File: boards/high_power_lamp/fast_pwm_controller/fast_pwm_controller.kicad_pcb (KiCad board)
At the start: 2 copper layers, 74 parts, among them J1 Screw_Terminal_01x02, J2 Screw_Terminal_01x02, J3 Screw_Terminal_01x02, J4 Screw_Terminal_01x02, J5 Screw_Terminal_01x02, J6 Screw_Terminal_01x02, J7 Screw_Terminal_01x02, J8 Screw_Terminal_01x02, J9 Screw_Terminal_01x02, Q1 BUK7516-55A,127, Q2 BUK7516-55A,127, Q3 BUK7516-55A,127, Q4 BUK7516-55A,127, U1 4050, U2 TLC3704, U3 SPX5205-adjustable, U4 ADA4851-4, U5 LMR380(10/20)

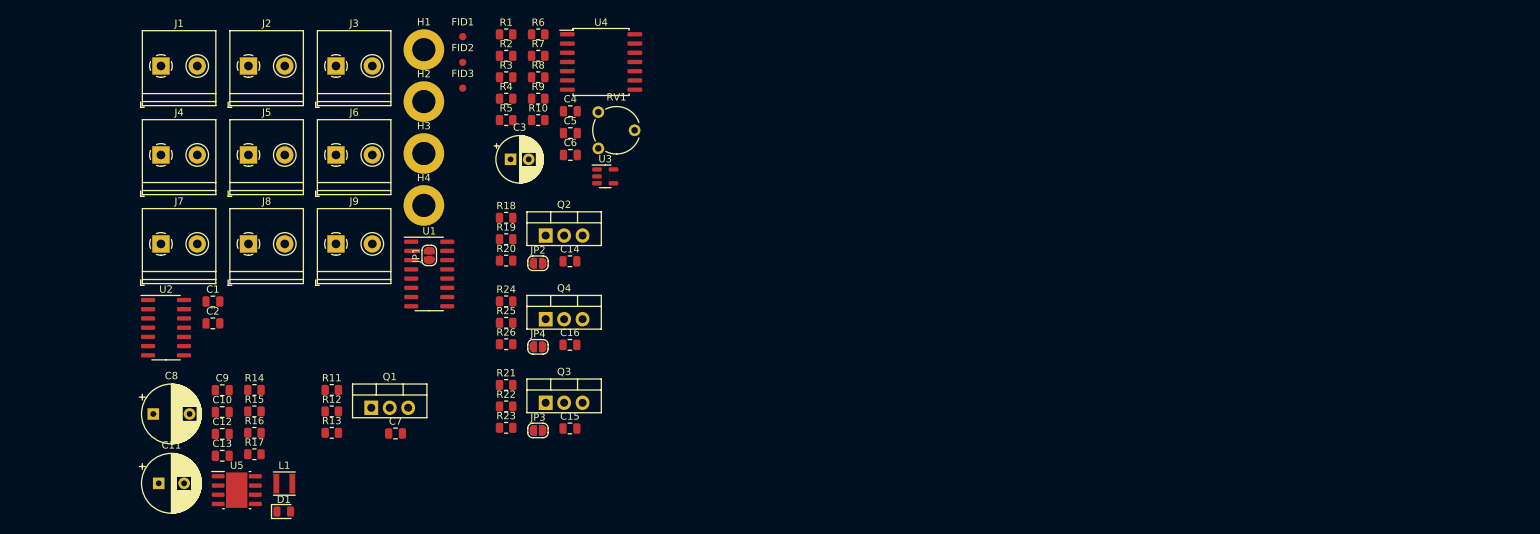
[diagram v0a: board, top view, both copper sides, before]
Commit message: buck converter can now be switched off via jumper
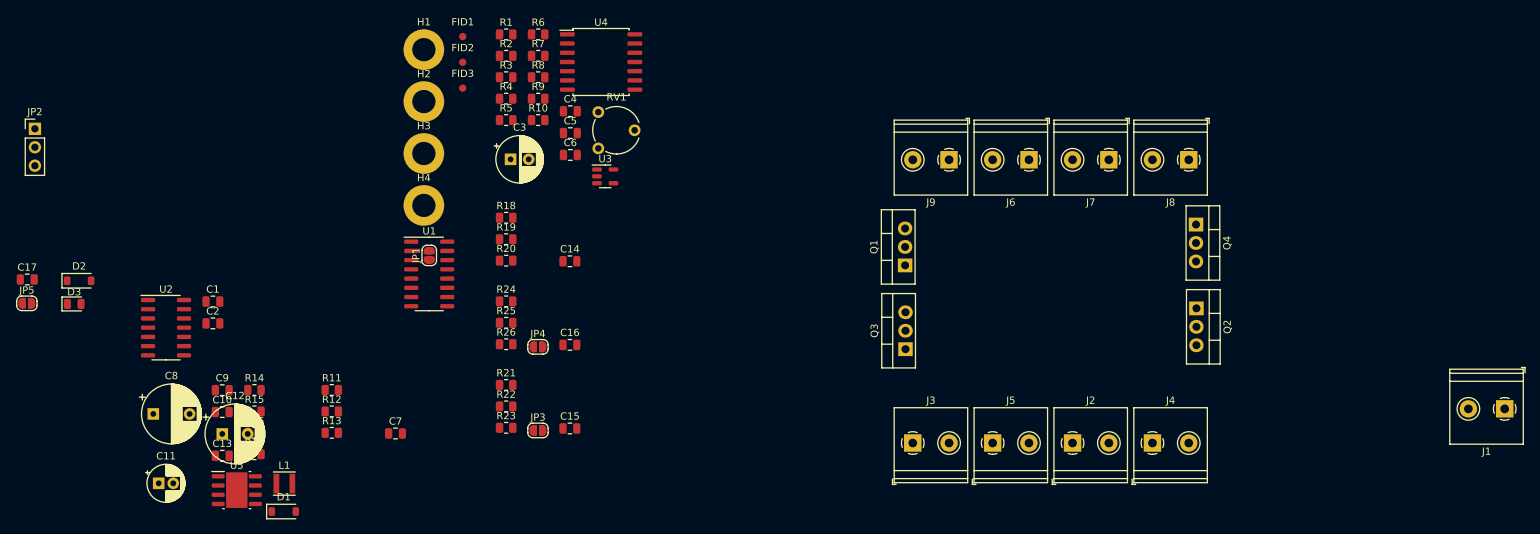
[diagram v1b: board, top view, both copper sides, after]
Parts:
- added C17: 500nF, Capacitor_SMD:C_0805_2012Metric, F.Cu at (43.1, 86.5)
- added D2: 1N4148, Diode_SMD:D_SOD-123, F.Cu at (50.2, 86.7)
- added D3: GREEN LED, LED_SMD:LED_0805_2012Metric, F.Cu at (49.5, 89.9)
- added JP5: SolderJumper_2_Open, Jumper:SolderJumper-2_P1.3mm_Open_RoundedPad1.0x1.5mm, F.Cu at (43.0, 89.8)
- C11: value 220μ -> 22μ; footprint Capacitor_THT:CP_Radial_D8.0mm_P3.50mm -> Capacitor_THT:CP_Radial_D5.0mm_P2.00mm
- C12: value 1μ -> 220μ; footprint Capacitor_SMD:C_0805_2012Metric -> Capacitor_THT:CP_Radial_D8.0mm_P3.50mm
- C13: value 100n -> 1μ
- C14: value 500nF -> 100n
- D1: value GREEN LED -> 1N4148; footprint LED_SMD:LED_0805_2012Metric -> Diode_SMD:D_SOD-123
- JP2: value SolderJumper_2_Open -> Jumper_3; footprint Jumper:SolderJumper-2_P1.3mm_Open_RoundedPad1.0x1.5mm -> Connector_PinHeader_2.54mm:PinHeader_1x03_P2.54mm_Vertical
- R15: value 100k -> 120k
- R16: value 9.09k -> 10.2k
- moved J1 190.9 mm to (246.5, 104.3), turned to 180 degrees
- moved J4 142.2 mm to (198.0, 109.0)
- moved J7 131.0 mm to (192.0, 70.0), turned to 180 degrees
- moved J8 130.0 mm to (203.0, 70.0), turned to 180 degrees
- moved J2 124.8 mm to (187.0, 109.0)
- moved J5 109.9 mm to (176.0, 109.0)
- moved J6 95.4 mm to (181.0, 70.0), turned to 180 degrees
- moved J3 94.9 mm to (165.0, 109.0)
- moved Q4 90.5 mm to (204.0, 78.9), turned to -90 degrees
- moved Q2 90.2 mm to (204.1, 90.5), turned to -90 degrees
- moved J9 85.2 mm to (170.0, 70.0), turned to 180 degrees
- moved Q1 76.1 mm to (163.9, 84.5), turned to 90 degrees
- moved JP2 71.7 mm to (44.1, 65.7)
- moved Q3 50.1 mm to (164.0, 96.1), turned to 90 degrees
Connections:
- C11 pad 1: +12V -> Net-(D2-A)
- C14 pad 1: GND -> +12V
- C14 pad 2: Net-(U2B-+) -> GND
- C15 pad 2: Net-(U2C-+) -> Net-(U2B-+)
- C16 pad 2: Net-(U2D-+) -> Net-(U2C-+)
- C8 pad 1: VPP -> Net-(D1-K)
- C9 pad 1: VPP -> Net-(JP2-A)
- D1 pad 1: GND -> Net-(D1-K)
- D1 pad 2: Net-(D1-A) -> VPP
- JP2 pad 1: /PWM stage 2/IN -> Net-(JP2-A)
- JP2 pad 2: Net-(JP2-B) -> Net-(D1-K)
- JP3 pad 1: /PWM stage 3/IN -> /PWM stage 2/IN
- JP4 pad 1: /PWM stage 4/IN -> /PWM stage 3/IN
- L1 pad 2: +12V -> Net-(D2-A)
- R15 pad 2: +12V -> Net-(D2-A)
- R17 pad 1: Net-(D1-A) -> Net-(D3-A)
- R19 pad 2: Net-(JP2-B) -> Net-(JP3-B)
- R22 pad 2: Net-(JP3-B) -> Net-(JP4-B)
- R25 pad 2: Net-(JP4-B) -> Net-(JP5-B)
- U1 pad 10: Net-(JP4-B) -> Net-(JP5-B)
- U1 pad 4: Net-(JP2-B) -> Net-(JP3-B)
- U1 pad 6: Net-(JP3-B) -> Net-(JP4-B)
- U5 pad 2: VPP -> Net-(JP2-A)
- U5 pad 3: VPP -> Net-(JP2-A)

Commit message: basic external layout of board
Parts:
- added H5: MountingHole, MountingHole:MountingHole_3.2mm_M3_DIN965_Pad, F.Cu at (50.0, 50.0)
- added H6: MountingHole, MountingHole:MountingHole_3.2mm_M3_DIN965_Pad, F.Cu at (50.0, 112.0)
- added H7: MountingHole, MountingHole:MountingHole_3.2mm_M3_DIN965_Pad, F.Cu at (112.0, 50.0)
- added H8: MountingHole, MountingHole:MountingHole_3.2mm_M3_DIN965_Pad, F.Cu at (112.0, 112.0)
- moved C3 199.9 mm to (199.7, -108.5)
- moved C7 199.9 mm to (183.9, -70.7)
- moved C8 199.9 mm to (150.5, -73.4)
- moved D2 199.9 mm to (140.3, -91.8)
- moved FID3 199.9 mm to (193.2, -118.3)
- moved JP2 199.9 mm to (134.2, -112.7)
- moved JP5 199.9 mm to (133.1, -88.7)
- moved L1 199.9 mm to (168.6, -63.8)
- moved R11 199.9 mm to (175.1, -76.7)
- moved U2 199.9 mm to (152.3, -85.3)
- moved C11 199.9 mm to (151.3, -63.9)
- moved C13 199.9 mm to (160.0, -67.7)
- moved C4 199.9 mm to (208.0, -115.1)
- moved FID1 199.9 mm to (193.2, -125.4)
- moved FID2 199.9 mm to (193.2, -121.8)
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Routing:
- net VPP: track 0.00 -> 61.3 mm
- net /PWM stage 1/OUT: track 0.00 -> 49.1 mm
- net /PWM stage 2/OUT: track 0.00 -> 40.2 mm
- net /PWM stage 4/OUT: track 0.00 -> 23.5 mm
- net /PWM stage 3/OUT: track 0.00 -> 17.4 mm
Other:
- board outline added: 72 x 72 mm

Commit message: almost finish arranging the fast pwm controller pcb
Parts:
- added C18: 500nF, Capacitor_SMD:C_0805_2012Metric, F.Cu at (80.6, 84.1)
- C11: value 22μ -> 100n; footprint Capacitor_THT:CP_Radial_D5.0mm_P2.00mm -> Capacitor_SMD:C_0805_2012Metric
- C12: value 220μ -> 22μ; footprint Capacitor_THT:CP_Radial_D8.0mm_P3.50mm -> Capacitor_THT:CP_Radial_D5.0mm_P2.00mm
- C13: value 1μ -> 220μ; footprint Capacitor_SMD:C_0805_2012Metric -> Capacitor_THT:CP_Radial_D8.0mm_P3.50mm
- C14: value 100n -> 1μ
- C15: value 500nF -> 100n
- C3: value 100μF -> 100nF; footprint Capacitor_THT:CP_Radial_D6.3mm_P2.50mm -> Capacitor_SMD:C_0805_2012Metric
- C4: value 100nF -> 100μF; footprint Capacitor_SMD:C_0805_2012Metric -> Capacitor_THT:CP_Radial_D6.3mm_P2.50mm
- C6: value 1nF -> 100nF
- C7: value 500nF -> 1nF
- C8: value 100μ -> 500nF; footprint Capacitor_THT:CP_Radial_D8.0mm_P5.00mm -> Capacitor_SMD:C_0805_2012Metric
- C9: value 100n -> 100μ; footprint Capacitor_SMD:C_0805_2012Metric -> Capacitor_THT:CP_Radial_D8.0mm_P5.00mm
- moved FID2 271.5 mm to (55.2, 112.1)
- moved R1 253.0 mm to (70.8, 92.4), turned to 180 degrees
- moved R2 251.5 mm to (74.3, 95.6), turned to 90 degrees
- moved U3 246.9 mm to (70.8, 95.9), turned to 90 degrees
- moved FID3 246.2 mm to (106.4, 112.1)
- moved C4 245.8 mm to (70.2, 88.5), turned to 90 degrees
- moved C14 244.8 mm to (58.7, 99.7), turned to 90 degrees
- moved C3 244.6 mm to (70.8, 99.4), turned to 180 degrees
- moved R18 243.2 mm to (64.8, 102.2)
- moved R7 239.4 mm to (90.8, 88.5)
- moved R8 234.6 mm to (90.8, 86.0)
- moved R5 234.0 mm to (90.8, 93.6), turned to 180 degrees
- moved U4 232.8 mm to (93.3, 78.3), turned to 90 degrees
- moved R24 231.1 mm to (69.2, 102.2), turned to 180 degrees
- moved RV1 227.9 mm to (99.7, 88.5), turned to 180 degrees
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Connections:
- C10 pad 1: Net-(U5-BOOT) -> Net-(JP2-A)
- C10 pad 2: /Power supply/PWR -> GND
- C11 pad 1: Net-(D2-A) -> Net-(U5-BOOT)
- C11 pad 2: GND -> /Power supply/PWR
- C12 pad 1: +12V -> Net-(D2-A)
- C15 pad 1: GND -> +12V
- C15 pad 2: Net-(U2B-+) -> GND
- C16 pad 2: Net-(U2C-+) -> Net-(U2B-+)
- C17 pad 2: Net-(U2D-+) -> Net-(U2C-+)
- C3 pad 1: /Triangle generator/TGEN_VCC -> GND
- C3 pad 2: GND -> +12V
- C4 pad 1: GND -> /Triangle generator/TGEN_VCC
- C4 pad 2: /Triangle generator/TGEN_VCC -> GND
- C5 pad 2: /Triangle generator/VMID -> /Triangle generator/TGEN_VCC
- C6 pad 1: Net-(U4A--) -> GND
- C6 pad 2: Net-(U4D-+) -> /Triangle generator/VMID
- C7 pad 1: GND -> Net-(U4A--)
- C7 pad 2: Net-(U2A-+) -> Net-(U4D-+)
- C8 pad 1: Net-(D1-K) -> GND
- C8 pad 2: GND -> Net-(U2A-+)
- C9 pad 1: Net-(JP2-A) -> Net-(D1-K)
- U1 pad 10: Net-(JP5-B) -> Net-(JP4-B)
- U1 pad 2: Net-(JP1-B) -> Net-(JP3-B)
- U1 pad 3: /PWM stage 1/IN -> /PWM stage 2/IN
- U1 pad 4: Net-(JP3-B) -> Net-(JP5-B)
- U1 pad 5: /PWM stage 2/IN -> /PWM stage 4/IN
- U1 pad 6: Net-(JP4-B) -> Net-(JP1-B)
- U1 pad 7: /PWM stage 3/IN -> /PWM stage 1/IN
- U1 pad 9: /PWM stage 4/IN -> /PWM stage 3/IN
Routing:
- net +12V: track 0.00 -> 100.1 mm
- net Net-(R20-Pad2): track 0.00 -> 80.3 mm
- net /Triangle generator/TGEN_VCC: track 0.00 -> 54.5 mm, vias 0 -> 3
- net Net-(R23-Pad2): track 0.00 -> 31.0 mm
- net /PWM stage 2/TRIANGLE: track 0.00 -> 28.6 mm, vias 0 -> 3
- net /PWM stage 2/IN: track 0.00 -> 28.3 mm
- net /PWM stage 3/IN: track 0.00 -> 26.8 mm
- net /PWM stage 4/IN: track 0.00 -> 26.7 mm, vias 0 -> 1
- net Net-(R26-Pad2): track 0.00 -> 26.1 mm
- net GND: track 0.00 -> 25.9 mm, vias 0 -> 7
- net /Triangle generator/VMID: track 0.00 -> 25.3 mm
- net Net-(U4D-+): track 0.00 -> 22.0 mm
- net /PWM stage 1/TRIANGLE: track 0.00 -> 20.2 mm, vias 0 -> 3
- net Net-(D2-A): track 0.00 -> 16.9 mm
- net /PWM stage 1/IN: track 0.00 -> 14.9 mm
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
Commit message: prepare traces
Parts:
- moved D1 2.22 mm to (59.1, 61.6)
- moved C9 2.11 mm to (59.1, 68.9)
- moved R23 1.31 mm to (109.5, 59.7)
- moved R20 1.27 mm to (109.2, 76.8)
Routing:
- net Net-(R20-Pad2): track 80.3 -> 40.8 mm
- net Net-(R13-Pad2): track 0.00 -> 38.6 mm
- net Net-(U2C-+): track 12.7 -> 24.4 mm, vias 0 -> 2
- net Net-(U2D-+): track 12.7 -> 23.4 mm, vias 0 -> 2
- net Net-(U2A-+): track 12.7 -> 18.9 mm
- net Net-(U2B-+): track 12.7 -> 17.9 mm
- net +12V: track 100.1 -> 102.7 mm
- net VPP: track 71.9 -> 69.7 mm
- net /PWM stage 2/TRIANGLE: track 28.6 -> 27.3 mm
- net Net-(D1-K): track 14.5 -> 13.6 mm

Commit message: arrange everything
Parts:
- moved R23 2.73 mm to (108.0, 61.9), turned to 180 degrees
- moved R20 1.27 mm to (109.2, 75.6)
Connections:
- C16 pad 2: Net-(U2B-+) -> Net-(U2C-+)
- C17 pad 2: Net-(U2C-+) -> Net-(U2B-+)
- C18 pad 2: Net-(U2D-+) -> Net-(U2A-+)
- C8 pad 2: Net-(U2A-+) -> Net-(U2D-+)
- Q1 pad 2: /PWM stage 1/OUT -> /PWM stage 3/OUT
- Q2 pad 2: /PWM stage 2/OUT -> /PWM stage 4/OUT
- Q3 pad 2: /PWM stage 3/OUT -> /PWM stage 2/OUT
- Q4 pad 2: /PWM stage 4/OUT -> /PWM stage 1/OUT
- R12 pad 1: Net-(U2A-+) -> Net-(U2D-+)
- R19 pad 1: Net-(U2B-+) -> Net-(U2C-+)
- R22 pad 1: Net-(U2C-+) -> Net-(U2B-+)
- R25 pad 1: Net-(U2D-+) -> Net-(U2A-+)
- R9 pad 2: /PWM stage 2/TRIANGLE -> /PWM stage 1/TRIANGLE
- U2 pad 1: Net-(R20-Pad2) -> Net-(R13-Pad2)
- U2 pad 10: /PWM stage 1/TRIANGLE -> /PWM stage 2/TRIANGLE
- U2 pad 2: Net-(R13-Pad2) -> Net-(R20-Pad2)
- U2 pad 4: /PWM stage 1/TRIANGLE -> /PWM stage 2/TRIANGLE
- U2 pad 6: /PWM stage 2/TRIANGLE -> /PWM stage 1/TRIANGLE
- U2 pad 8: /PWM stage 2/TRIANGLE -> /PWM stage 1/TRIANGLE
- U4 pad 13: /PWM stage 1/TRIANGLE -> /PWM stage 2/TRIANGLE
- U4 pad 14: /PWM stage 1/TRIANGLE -> /PWM stage 2/TRIANGLE
- U4 pad 8: /PWM stage 2/TRIANGLE -> /PWM stage 1/TRIANGLE
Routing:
- net Net-(Q3-G): track 0.00 -> 8.26 mm
- net /PWM stage 2/TRIANGLE: track 27.3 -> 20.2 mm
- net /PWM stage 1/TRIANGLE: track 20.2 -> 27.3 mm
- net Net-(Q1-G): track 0.00 -> 5.70 mm
- net Net-(R13-Pad2): track 38.6 -> 42.7 mm
- net Net-(Q4-G): track 0.00 -> 3.56 mm
- net Net-(Q2-G): track 0.00 -> 3.47 mm
- net Net-(U2C-+): track 24.4 -> 26.6 mm
- net Net-(U2D-+): track 23.4 -> 25.6 mm
- net Net-(U2A-+): track 18.9 -> 21.2 mm
- net Net-(U2B-+): track 17.9 -> 20.1 mm
- net Net-(R20-Pad2): track 40.8 -> 38.6 mm
- net Net-(R23-Pad2): track 31.0 -> 29.2 mm
- net Net-(R26-Pad2): track 26.1 -> 26.6 mm

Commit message: finalise connections
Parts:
- moved C10 12.7 mm to (55.9, 76.5), turned to 90 degrees
- moved C11 5.37 mm to (60.0, 88.6)
- moved JP2 3.51 mm to (60.0, 76.5)
- moved C12 2.24 mm to (64.1, 94.6)
- moved R14 0.63 mm to (54.0, 81.5)
- moved Q4 0.33 mm to (48.6, 61.5)
- moved Q1 0.32 mm to (48.6, 80.5)
- moved R2 0.32 mm to (74.3, 95.2)
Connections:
- J6 pad 2: /PWM stage 1/OUT -> /PWM stage 3/OUT
- J7 pad 2: /PWM stage 2/OUT -> /PWM stage 4/OUT
- J8 pad 2: /PWM stage 3/OUT -> /PWM stage 2/OUT
- J9 pad 2: /PWM stage 4/OUT -> /PWM stage 1/OUT
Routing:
- net /PWM stage 3/OUT: track 17.4 -> 47.9 mm
- net /PWM stage 1/OUT: track 48.2 -> 23.2 mm
- net /PWM stage 2/OUT: track 40.2 -> 17.4 mm
- net /PWM stage 4/OUT: track 23.5 -> 40.2 mm
- net Net-(JP2-A): track 5.68 -> 8.91 mm
- net Net-(D2-A): track 16.9 -> 14.2 mm
- net +12V: track 102.7 -> 100.3 mm
- net Net-(R13-Pad2): track 42.7 -> 40.8 mm
- net Net-(R20-Pad2): track 38.6 -> 37.3 mm
- net Net-(D1-K): track 13.6 -> 14.7 mm
- net Net-(U5-RT/SYNC): track 2.24 -> 2.87 mm
- net GND: track 25.9 -> 26.3 mm, vias 7 -> 51
- added copper zone on B.Cu, net GND
- added copper zone on F.Cu, net GND

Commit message: finalise board
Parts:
- added TP1: TestPoint, TestPoint:TestPoint_THTPad_D2.0mm_Drill1.0mm, F.Cu at (100.6, 70.8)
- added TP10: TestPoint, TestPoint:TestPoint_THTPad_D2.0mm_Drill1.0mm, F.Cu at (91.1, 65.1)
- added TP2: TestPoint, TestPoint:TestPoint_THTPad_D2.0mm_Drill1.0mm, F.Cu at (87.6, 70.8)
- added TP3: TestPoint, TestPoint:TestPoint_THTPad_D2.0mm_Drill1.0mm, F.Cu at (81.9, 77.8)
- added TP4: TestPoint, TestPoint:TestPoint_THTPad_D2.0mm_Drill1.0mm, F.Cu at (89.5, 61.0)
- added TP5: TestPoint, TestPoint:TestPoint_THTPad_D2.0mm_Drill1.0mm, F.Cu at (76.8, 77.8)
- added TP6: TestPoint, TestPoint:TestPoint_THTPad_D2.0mm_Drill1.0mm, F.Cu at (92.7, 61.0)
- added TP7: TestPoint, TestPoint:TestPoint_THTPad_D2.0mm_Drill1.0mm, F.Cu at (84.5, 75.2)
- added TP8: TestPoint, TestPoint:TestPoint_THTPad_D2.0mm_Drill1.0mm, F.Cu at (71.1, 68.3)
- added TP9: TestPoint, TestPoint:TestPoint_THTPad_D2.0mm_Drill1.0mm, F.Cu at (79.4, 75.2)
- renumbered J9 to J6, J8 to J7, J6 to J8, J7 to J9, Q4 to Q1, Q3 to Q2, Q1 to Q3, Q2 to Q4, R26 to R13, R23 to R20, R13 to R23, R20 to R26
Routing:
- net Net-(R13-Pad2): track 26.6 -> 40.1 mm
- net GND: track 26.3 -> 20.3 mm, vias 51 -> 83
- net /PWM stage 2/TRIANGLE: track 20.2 -> 23.3 mm
- net /PWM stage 1/TRIANGLE: track 27.3 -> 30.3 mm
- net Net-(R20-Pad2): track 29.2 -> 32.0 mm
- net Net-(R23-Pad2): track 40.8 -> 43.6 mm
- net Net-(R26-Pad2): track 37.3 -> 39.5 mm

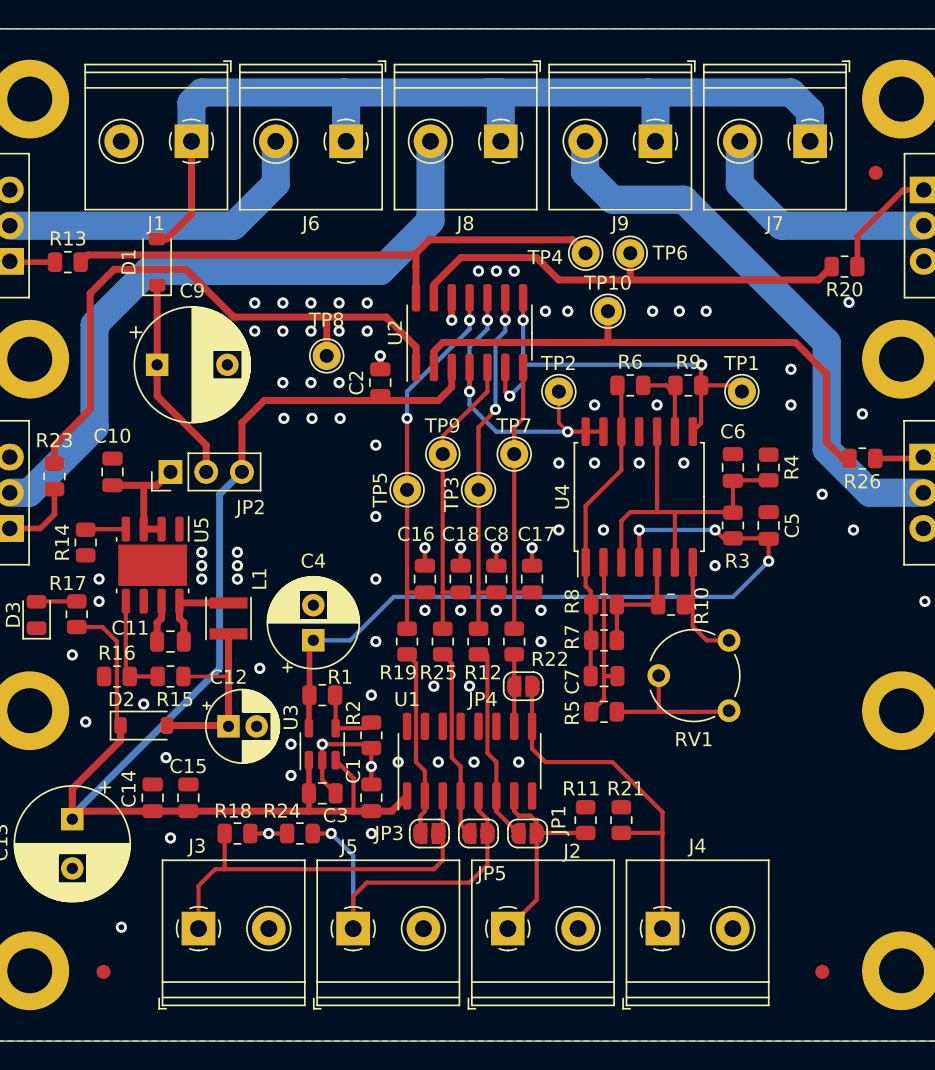
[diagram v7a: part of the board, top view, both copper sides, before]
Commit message: change connectors
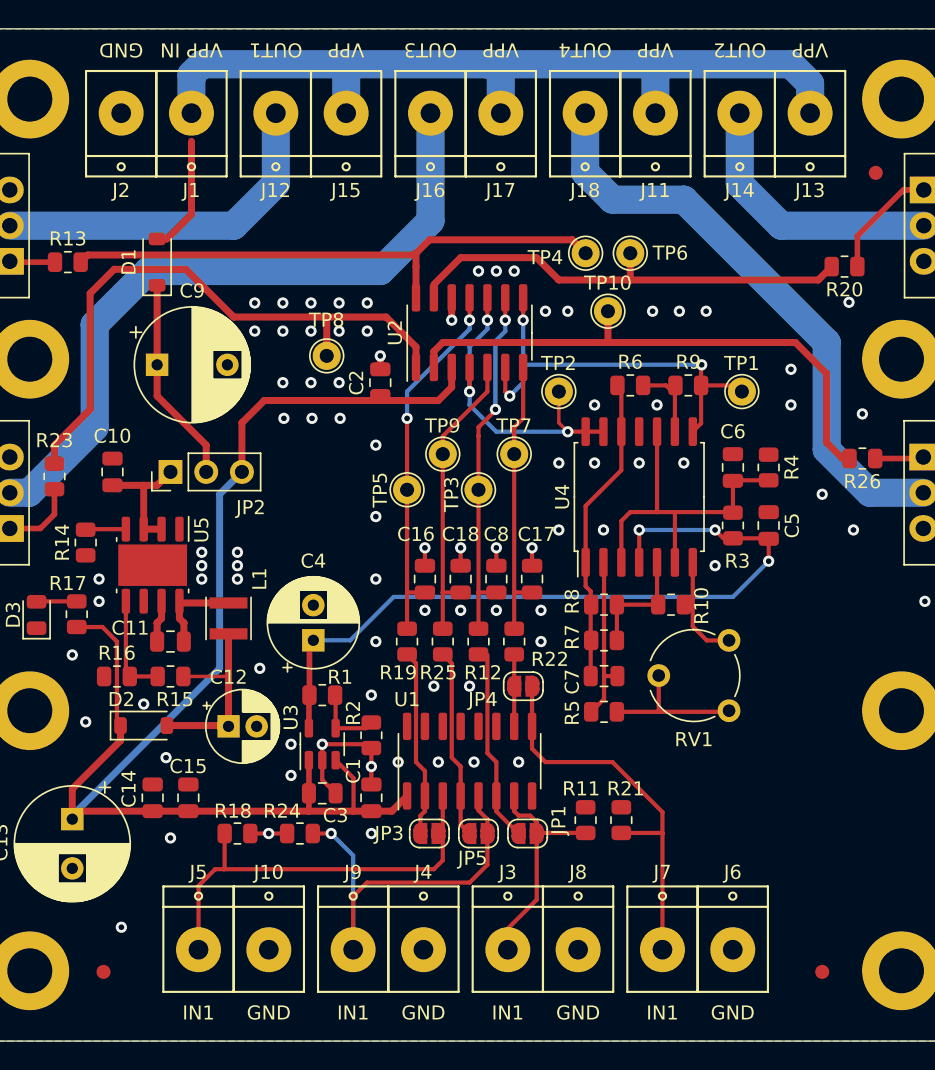
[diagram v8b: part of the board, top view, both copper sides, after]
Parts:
- added J10: Screw_Terminal_01x01, connectors:1PIN_DG306, F.Cu at (67.0, 110.5)
- added J11: Screw_Terminal_01x01, connectors:1PIN_DG306, F.Cu at (94.5, 51.0)
- added J12: Screw_Terminal_01x01, connectors:1PIN_DG306, F.Cu at (67.5, 51.0)
- added J13: Screw_Terminal_01x01, connectors:1PIN_DG306, F.Cu at (105.5, 51.0)
- added J14: Screw_Terminal_01x01, connectors:1PIN_DG306, F.Cu at (100.5, 51.0)
- added J15: Screw_Terminal_01x01, connectors:1PIN_DG306, F.Cu at (72.5, 51.0)
- added J16: Screw_Terminal_01x01, connectors:1PIN_DG306, F.Cu at (78.5, 51.0)
- added J17: Screw_Terminal_01x01, connectors:1PIN_DG306, F.Cu at (83.5, 51.0)
- added J18: Screw_Terminal_01x01, connectors:1PIN_DG306, F.Cu at (89.5, 51.0)
- J1, J2, J3, J4, J5, J6, J7, J8, J9: value Screw_Terminal_01x02 -> Screw_Terminal_01x01; footprint TerminalBlock_Philmore:TerminalBlock_Philmore_TB132_1x02_P5.00mm_Horizontal -> connectors:1PIN_DG306
- moved J2 64.2 mm to (56.5, 51.0)
- moved J6 63.7 mm to (100.0, 110.5)
- moved J9 61.4 mm to (73.0, 110.5)
- moved J7 58.5 mm to (95.0, 110.5)
- moved J8 57.8 mm to (89.0, 110.5)
- moved J3 22.1 mm to (84.0, 110.5), turned to 180 degrees
- moved J4 17.1 mm to (78.0, 110.5), turned to 180 degrees
- moved J5 11.1 mm to (62.0, 110.5), turned to 180 degrees
- moved J1 2.00 mm to (61.5, 51.0), turned to 0 degrees
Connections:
- J2 pad 1: /PWM stage 1/IN -> GND
- J3 pad 1: /PWM stage 2/IN -> /PWM stage 1/IN
- J4 pad 1: /PWM stage 3/IN -> GND
- J5 pad 1: /PWM stage 4/IN -> /PWM stage 2/IN
- J6 pad 1: VPP -> GND
- J7 pad 1: VPP -> /PWM stage 3/IN
- J8 pad 1: VPP -> GND
- J9 pad 1: VPP -> /PWM stage 4/IN
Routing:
- net /PWM stage 4/OUT: track 40.2 -> 42.2 mm
- net /PWM stage 2/OUT: track 17.4 -> 19.4 mm
- net /PWM stage 1/OUT: track 23.2 -> 25.2 mm
- net /PWM stage 3/OUT: track 47.9 -> 49.9 mm
